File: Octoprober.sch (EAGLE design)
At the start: 143 parts, among them J1 10118193-0001LF, J2 26-60-4020, SW1 EVQ-Q2203W, SW2 EVQ-Q2203W, SW3 EVQ-Q2203W, SW4 EVQ-Q2203W, SW5 EVQ-Q2203W, U1 P8X32A-M44, U10 MAX31855KASA+, U11 MAX31855KASA+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

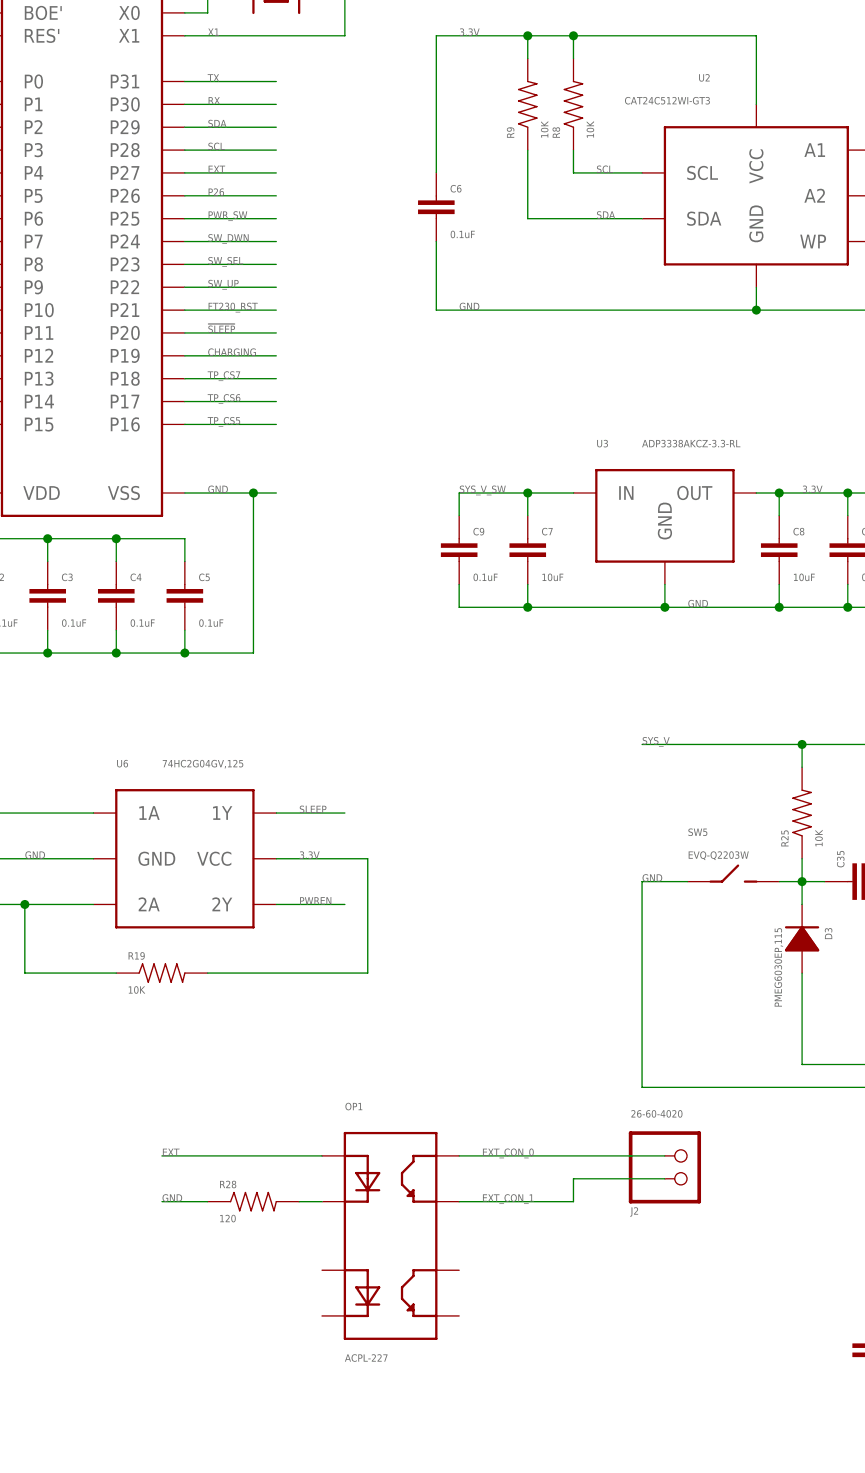
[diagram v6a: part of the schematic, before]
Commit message: REV1 finished routing. Need to increase font size.
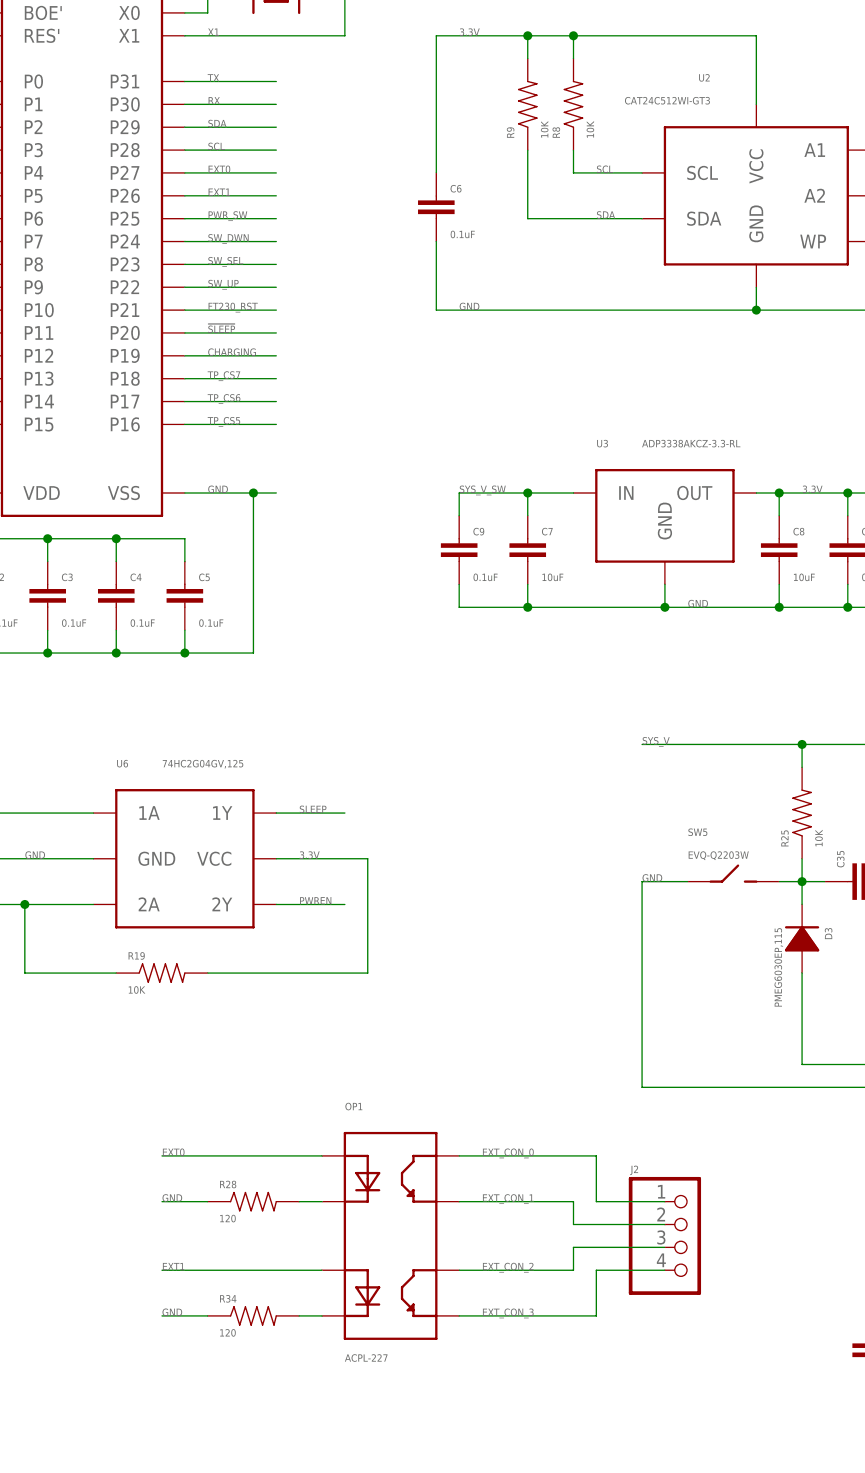
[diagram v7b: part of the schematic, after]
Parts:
- added R34: 120, PP_Passives:RESISTOR0402
- J2: value 26-60-4020 -> (none); device PP_Connectors:PH_1X02MOLEX_26-61-4020 -> PP_Connectors:PH_1X04HEADER_PTH
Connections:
- net EXT renamed EXT0
- removed net P26: U1.P26
- new net EXT1: OP1.3, U1.P26
- new net EXT_CON_2: J2.3, OP1.6
- new net EXT_CON_3: J2.4, OP1.5
- new net N$24: OP1.4, R34.2
- net EXT_CON_0: now also J2.1; no longer J2.2
- net EXT_CON_1: now also J2.2; no longer J2.1
- net GND: now also R34.1
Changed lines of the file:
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@@
 <part name="R27" library="PP_Passives" deviceset="RESISTOR" device="0402" value="300K"/>
 <part name="U$2" library="PP_Aesthetics" deviceset="OCTOPROBER_LOGO" device="NORMAL"/>
-<part name="J2" library="PP_Connectors" deviceset="PH_1X02" device="MOLEX_26-61-4020" value="26-60-4020"/>
 <part name="OP1" library="PP_DigitalIC" deviceset="ACPL-227" device="SOIC-8" value="ACPL-227"/>
 <part name="R28" library="PP_Passives" deviceset="RESISTOR" device="0402" value="120"/>
@@
 <part name="R32" library="PP_Passives" deviceset="RESISTOR" device="0402" value="330"/>
 <part name="R33" library="PP_Passives" deviceset="RESISTOR" device="0402" value="10K"/>
+<part name="R34" library="PP_Passives" deviceset="RESISTOR" device="0402" value="120"/>
+<part name="J2" library="PP_Connectors" deviceset="PH_1X04" device="HEADER_PTH"/>
 </parts>
 <sheets>
@@
 <instance part="R27" gate="G$1" x="132.08" y="-76.2" rot="R180"/>
 <instance part="U$2" gate="G$1" x="-284.48" y="-101.6"/>
-<instance part="J2" gate="G$1" x="63.5" y="-99.06" rot="MR180"/>
 <instance part="OP1" gate="G$1" x="33.02" y="-104.14"/>
 <instance part="R28" gate="G$1" x="17.78" y="-101.6"/>
@@
 <instance part="R32" gate="G$1" x="93.98" y="-22.86"/>
 <instance part="R33" gate="G$1" x="-22.86" y="-45.72" rot="R270"/>
+<instance part="R34" gate="G$1" x="17.78" y="-114.3"/>
+<instance part="J2" gate="G$1" x="63.5" y="-101.6"/>
 </instances>
 <busses>
@@
 </segment>
 </net>
-<net name="EXT" class="0">
+<net name="EXT0" class="0">
 <segment>
 <pinref part="U1" gate="G$1" pin="P27"/>
@@
 <wire x1="-139.7" y1="30.48" x2="-147.32" y2="30.48" width="0.1524" layer="91"/>
 <label x="-147.32" y="30.48" size="0.8128" layer="95" font="vector"/>
+</segment>
+<segment>
+<pinref part="R34" gate="G$1" pin="1"/>
+<wire x1="12.7" y1="-114.3" x2="7.62" y2="-114.3" width="0.1524" layer="91"/>
+<label x="7.62" y="-114.3" size="0.8128" layer="95" font="vector"/>
 </segment>
 </net>
@@
 <wire x1="40.64" y1="-101.6" x2="53.34" y2="-101.6" width="0.1524" layer="91"/>
 <label x="43.18" y="-101.6" size="0.8128" layer="95" font="vector"/>
-<wire x1="53.34" y1="-99.06" x2="53.34" y2="-101.6" width="0.1524" layer="91"/>
-<pinref part="J2" gate="G$1" pin="1"/>
-<wire x1="63.5" y1="-99.06" x2="53.34" y2="-99.06" width="0.1524" layer="91"/>
+<wire x1="53.34" y1="-101.6" x2="53.34" y2="-104.14" width="0.1524" layer="91"/>
+<pinref part="J2" gate="G$1" pin="2"/>
+<wire x1="53.34" y1="-104.14" x2="63.5" y2="-104.14" width="0.1524" layer="91"/>
 </segment>
 </net>
@@
 <pinref part="OP1" gate="G$1" pin="8"/>
 <label x="43.18" y="-96.52" size="0.8128" layer="95" font="vector"/>
-<wire x1="40.64" y1="-96.52" x2="63.5" y2="-96.52" width="0.1524" layer="91"/>
-<pinref part="J2" gate="G$1" pin="2"/>
+<wire x1="40.64" y1="-96.52" x2="55.88" y2="-96.52" width="0.1524" layer="91"/>
+<wire x1="55.88" y1="-96.52" x2="55.88" y2="-101.6" width="0.1524" layer="91"/>
+<pinref part="J2" gate="G$1" pin="1"/>
+<wire x1="55.88" y1="-101.6" x2="63.5" y2="-101.6" width="0.1524" layer="91"/>
 </segment>
 </net>
@@
 </segment>
 </net>
-<net name="P26" class="0">
+<net name="EXT1" class="0">
 <segment>
 <pinref part="U1" gate="G$1" pin="P26"/>
@@
 <label x="12.7" y="10.16" size="0.8128" layer="95" font="vector"/>
 </segment>
-</net>
+<segment>
+<pinref part="OP1" gate="G$1" pin="3"/>
+<wire x1="25.4" y1="-109.22" x2="7.62" y2="-109.22" width="0.1524" layer="91"/>
+<label x="7.62" y="-109.22" size="0.8128" layer="95" font="vector"/>
+</segment>
+</net>
+<net name="N$24" class="0">
+<segment>
+<pinref part="OP1" gate="G$1" pin="4"/>
+<pinref part="R34" gate="G$1" pin="2"/>
+<wire x1="25.4" y1="-114.3" x2="22.86" y2="-114.3" width="0.1524" layer="91"/>
+</segment>
+</net>
+<net name="EXT_CON_2" class="0">
+<segment>
+<pinref part="OP1" gate="G$1" pin="6"/>
+<wire x1="40.64" y1="-109.22" x2="53.34" y2="-109.22" width="0.1524" layer="91"/>
+<label x="43.18" y="-109.22" size="0.8128" layer="95" font="vector"/>
+<wire x1="53.34" y1="-109.22" x2="53.34" y2="-106.68" width="0.1524" layer="91"/>
+<pinref part="J2" gate="G$1" pin="3"/>
+<wire x1="53.34" y1="-106.68" x2="63.5" y2="-106.68" width="0.1524" layer="91"/>
+</segment>
+</net>
+<net name="EXT_CON_3" class="0">
+<segment>
+<pinref part="OP1" gate="G$1" pin="5"/>
+<wire x1="40.64" y1="-114.3" x2="55.88" y2="-114.3" width="0.1524" layer="91"/>
+<label x="43.18" y="-114.3" size="0.8128" layer="95" font="vector"/>
+<wire x1="55.88" y1="-114.3" x2="55.88" y2="-109.22" width="0.1524" layer="91"/>
+<pinref part="J2" gate="G$1" pin="4"/>
+<wire x1="55.88" y1="-109.22" x2="63.5" y2="-109.22" width="0.1524" layer="91"/>
+</segment>
+</net>
